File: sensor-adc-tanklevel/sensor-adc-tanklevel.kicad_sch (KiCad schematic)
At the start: 13 parts, among them J2 ESP-01S, U1 LMZM23601V3SILR, U2 ADS1115

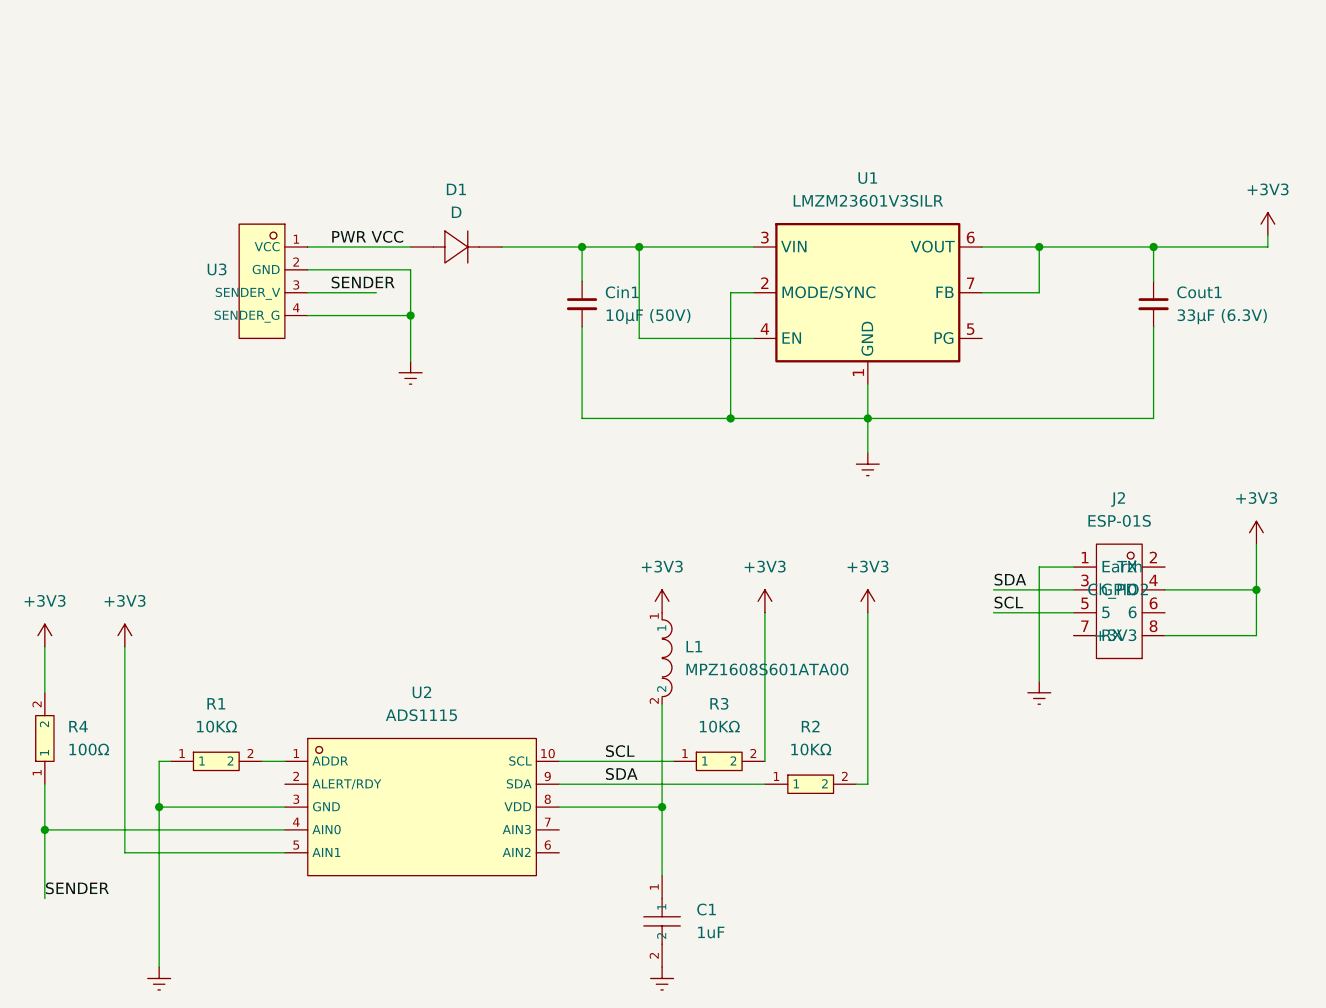
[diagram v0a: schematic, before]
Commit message: Replaced LMZM23601V3SILR with AP63203WU-7
It turned out that the price of the TI LMZM23601V3SILR. Replaced
this with cheaper one. I hope it works...
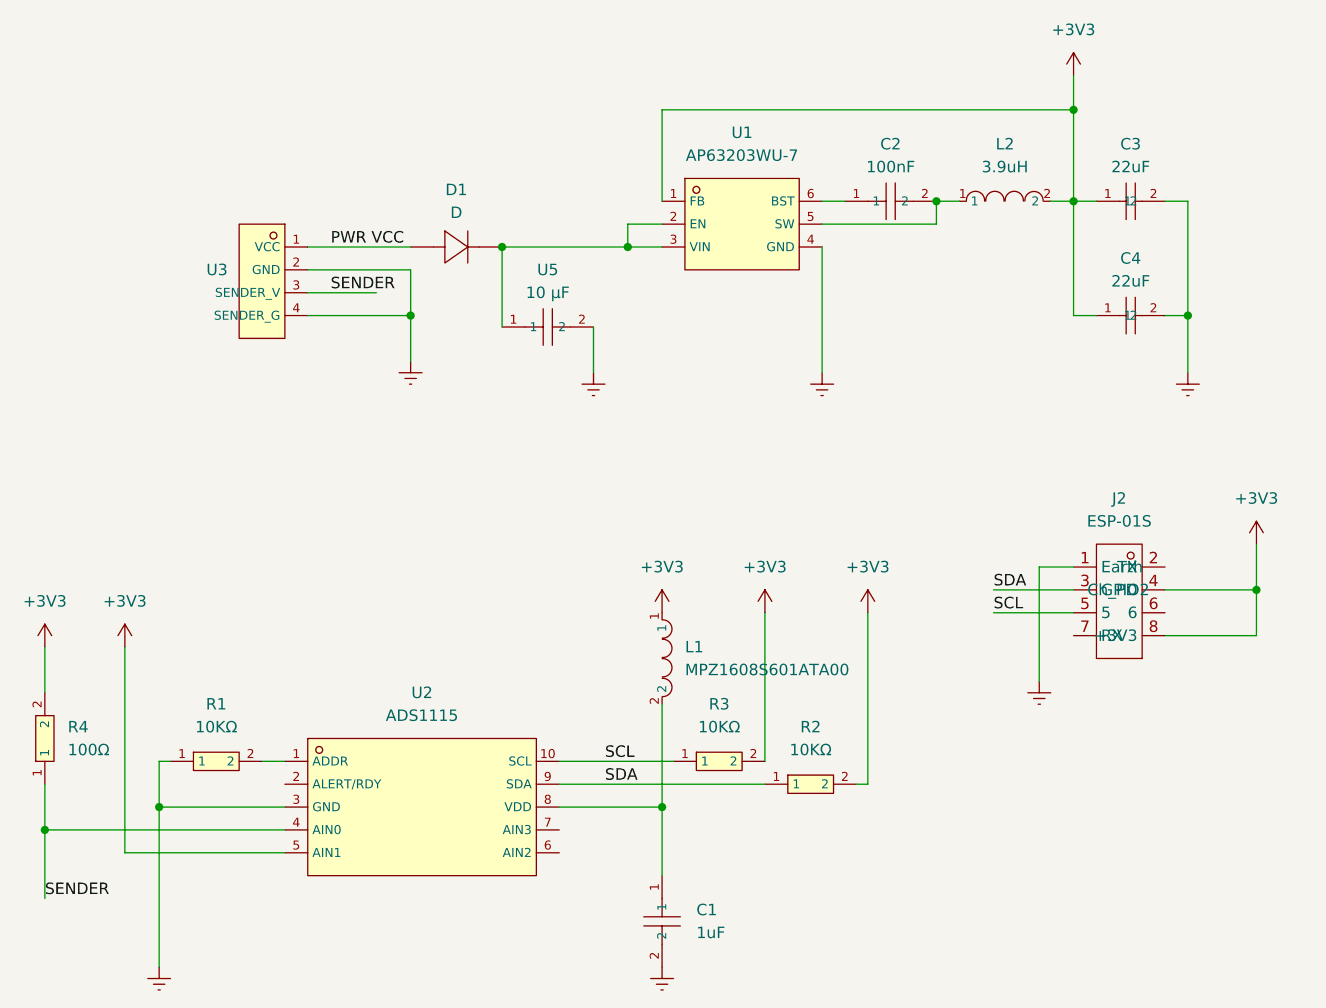
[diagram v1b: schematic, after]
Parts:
- removed Cin1: 10μF (50V), Capacitor_SMD:C_1210_3225Metric, symbol Device:C_Small
- removed Cout1: 33μF (6.3V), Capacitor_SMD:C_1210_3225Metric, symbol Device:C_Small
- removed U1: LMZM23601V3SILR, Package_LGA:Texas_SIL0010A_MicroSiP-10-1EP_3.8x3mm_P0.6mm_EP0.7x2.9mm_ThermalVias, symbol Regulator_Switching:LMZM23601
- added C2: 100nF, lcsc_footprints:C1525_C0402, symbol LCSC:100nF_(104)_±10%_16V
- added C3, C4: 22uF, lcsc_footprints:C12891_C1206, symbol LCSC:22uF_(226)_±10%_25V
- added L2: 3.9uH, lcsc_footprints:C57836_L0603, symbol LCSC:3_9uH
- added U1: AP63203WU-7, lcsc_footprints:C780769_TSOT-26_L2_9-W1_6-P0_95-LS2_8-BL, symbol LCSC:AP63203WU-7
- added U5: 10 µF, lcsc_footprints:C22367827_C0603, symbol LCSC:HGC0603R5106M350NTHJ
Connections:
- net +3V3: now also C3.1, C4.1, L2.2, U1.1 (FB)
- net Earth: now also C3.2, C4.2, U1.4 (GND), U5.2
- net at D1.1 (K): now also U1.2 (EN), U1.3 (VIN), U5.1
- new net: C2.2, L2.1, U1.5 (SW)
- new net: C2.1, U1.6 (BST)

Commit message: Changed all symbols and footprints to LCSC versions
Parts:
- CN2: renamed from J2; value ESP-01S -> PM254-2-04-S-8.5; footprint C3975149:HDR-SMD_8P-P2.54-V-F-R2-C4-S7.1 -> lcsc_footprints:C3975149_HDR-SMD_8P-P2_54-V-F-R2-C4-S7_1; symbol C3975149:PM254-2-04-S-8.5 -> lcsc_imported:PM254-2-04-S-8_5
- D1: value D -> S7116-300A; footprint C5174649:SOD-323_L1.7-W1.3-LS2.5-RD -> lcsc_footprints:C5174649_SOD-323_L1_7-W1_3-LS2_5-RD; symbol C5174649:S7116-300A -> LCSC:S7116-300A
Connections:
- net +3V3: now also CN2.3, CN2.7; no longer CN2.4 (Ch_PD), CN2.8 (+3V3)
- net Earth: now also CN2.2; no longer CN2.1 (Earth)
- net SCL: now also CN2.6; no longer CN2.5
- net SDA: now also CN2.4; no longer CN2.3 (GPIO2)

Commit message: Minor finishing touches before production
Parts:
- renumbered U3 to CN1
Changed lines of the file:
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@@
 	(title_block
 		(title "Nemo-K Tank Sensor (AD1115)")
-		(date "2026-10-30")
+		(date "2026-11-01")
 		(rev "v1")
 		(company "Sivuduuni Global Oy")
@@
 		(in_pos_files yes)
 		(dnp no)
-		(property "Reference" "U3"
+		(property "Reference" "CN1"
 			(at 77.47 80.0099 0)
 			(show_name no)
@@
 			(project "sensor-adc-tanklevel"
 				(path "/9538e4ed-27e6-4c37-b989-9859dc0d49e8"
-					(reference "U3")
+					(reference "CN1")
 					(unit 1)
 				)

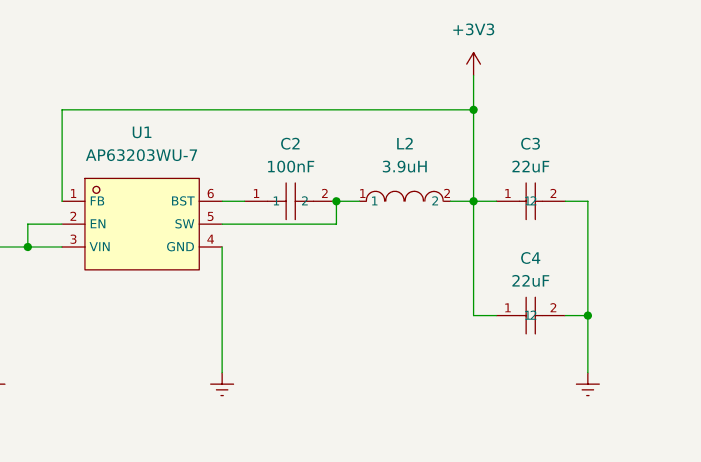
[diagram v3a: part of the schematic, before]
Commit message: Changed L2 coil as the previous was not available
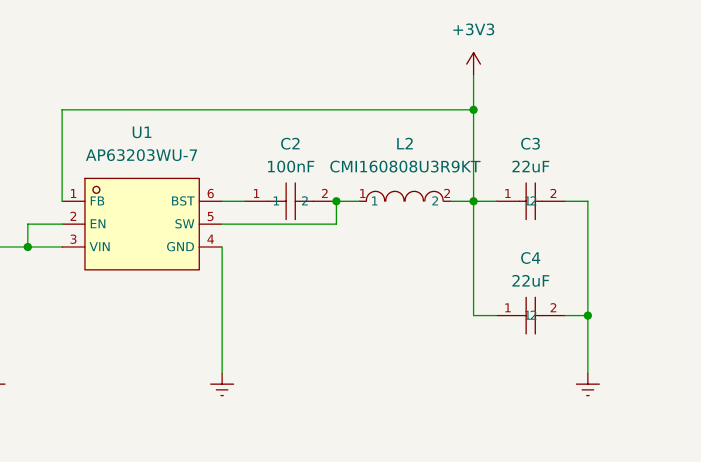
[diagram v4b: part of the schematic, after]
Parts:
- L2: value 3.9uH -> CMI160808U3R9KT; footprint lcsc_footprints:C57836_L0603 -> lcsc_footprints:C139210_L0603; symbol LCSC:3_9uH -> LCSC:CMI160808U3R9KT; LCSC C57836 -> C139210; Manufacturer Sunlord(顺络) -> FH(风华)
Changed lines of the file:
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@@
 	)
 	(symbol
-		(lib_id "LCSC:3_9uH")
+		(lib_id "LCSC:CMI160808U3R9KT")
 		(at 163.83 72.39 0)
 		(unit 1)
@@
 			)
 		)
-		(property "Value" "3.9uH"
+		(property "Value" "CMI160808U3R9KT"
 			(at 163.83 68.58 0)
 			(show_name no)
@@
 			)
 		)
-		(property "Footprint" "lcsc_footprints:C57836_L0603"
+		(property "Footprint" "lcsc_footprints:C139210_L0603"
 			(at 163.83 82.55 0)
 			(hide yes)
@@
 			)
 		)
-		(property "Datasheet" "https://wmsc.lcsc.com/wmsc/upload/file/pdf/v2/lcsc/2310301641_Sunlord-SDFL1608Q3R9KTF_C57836.pdf"
+		(property "Datasheet" "https://www.lcsc.com/datasheet/lcsc_datasheet_2302231230_FH--Guangdong-Fenghua-Advanced-Tech-CMI160808U3R9KT_C139210.pdf"
 			(at 161.544 72.263 0)
 			(hide yes)
@@
 			)
 		)
-		(property "Description" "3.9uH"
+		(property "Description" "CMI160808U3R9KT"
 			(at 163.83 72.39 0)
 			(hide yes)
@@
 			)
 		)
-		(property "LCSC" "C57836"
+		(property "LCSC" "C139210"
 			(at 163.83 72.39 0)
 			(hide yes)
@@
 			)
 		)
-		(property "Manufacturer" "Sunlord(顺络)"
+		(property "Manufacturer" "FH(风华)"
 			(at 163.83 72.39 0)
 			(hide yes)
